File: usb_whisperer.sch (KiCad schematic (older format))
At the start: 2 parts, among them J1 Conn_01x04, J9 Conn_01x04

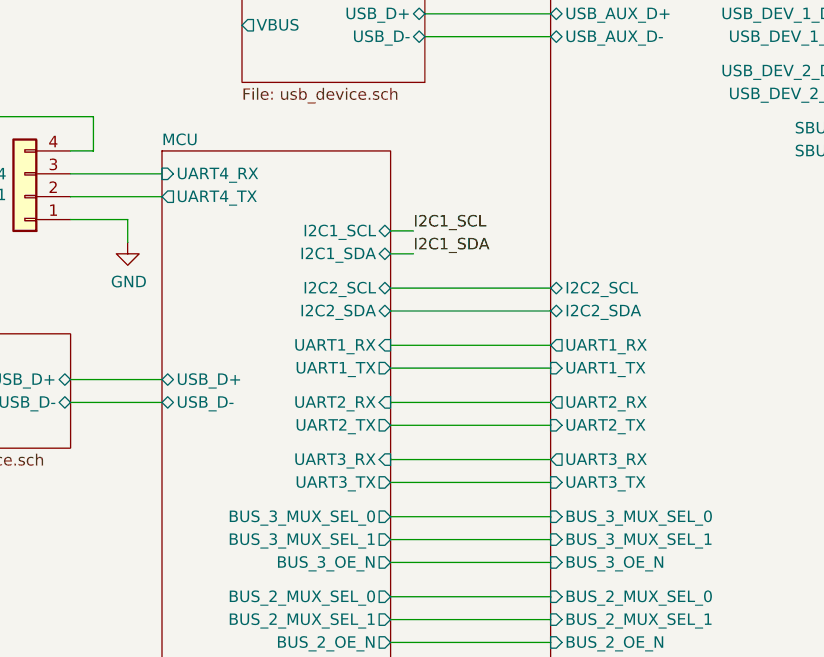
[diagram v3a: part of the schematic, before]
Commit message: Replace MCU by something available in distributors
Given the current chip shortage the STM32F0 was not available from
JLCPCB. This one (STM32F411CE) is available in large quantities from
JLCPCB. Despite being much more powerful than the F0, it is still in the
price range and actually cheaper than the STM32F103C8T6... which I don't
understand...
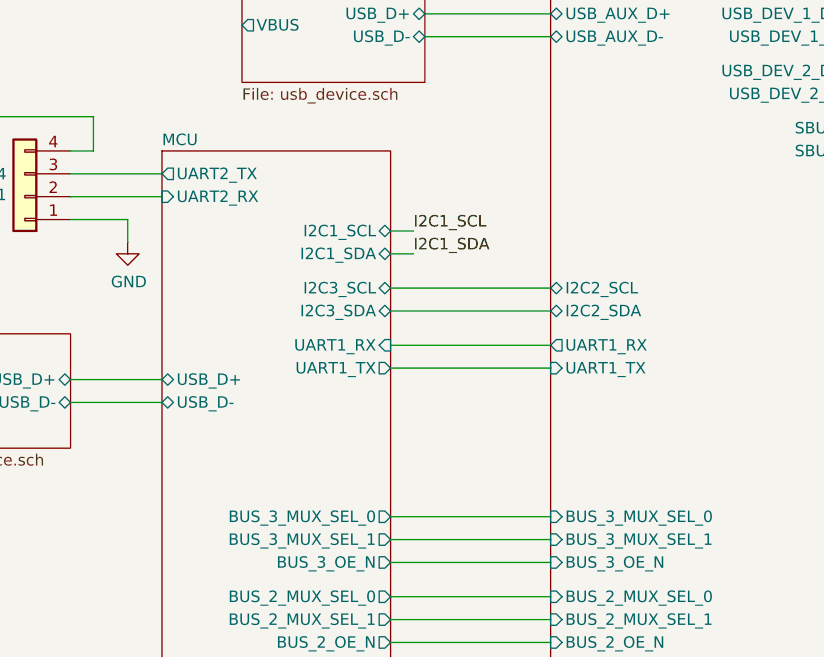
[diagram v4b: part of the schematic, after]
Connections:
- net MCU/UART4_RX is gone; now on net MCU/UART2_TX: J1.3 (Pin_3)
- net MCU/UART4_TX is gone; now on net MCU/UART2_RX: J1.2 (Pin_2)
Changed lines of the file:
@@
 F8 "UART1_TX" I L 5900 3850 50
 F9 "UART1_RX" O L 5900 3750 50
-F10 "UART2_TX" I L 5900 4100 50
-F11 "UART2_RX" O L 5900 4000 50
-F12 "UART3_TX" I L 5900 4350 50
-F13 "UART3_RX" O L 5900 4250 50
 F14 "I2C2_SCL" B L 5900 3500 50
 F15 "I2C2_SDA" B L 5900 3600 50
@@
 	5200 3850 5900 3850
 Wire Wire Line
-	5900 4000 5200 4000
-Wire Wire Line
-	5200 4100 5900 4100
-Wire Wire Line
 	7250 2300 8050 2300
 Wire Wire Line
@@
 Wire Wire Line
 	7650 3050 8050 3050
+Wire Wire Line
+	3800 3100 4200 3100
+Wire Wire Line
+	4200 3000 3800 3000
+$Comp
+L power:GND #PWR01
+U 1 1 61C1F3C5
+P 4050 3300
+F 0 "#PWR01" H 4050 3050 50  0001 C CNN
+F 1 "GND" H 4055 3127 50  0000 C CNN
+F 2 "" H 4050 3300 50  0001 C CNN
+F 3 "" H 4050 3300 50  0001 C CNN
+	1    4050 3300
+	1    0    0    -1
+$EndComp
+Wire Wire Line
+	4050 3300 4050 3200
+Wire Wire Line
+	4050 3200 3800 3200
+Wire Wire Line
+	5300 3250 5200 3250
+Wire Wire Line
+	5200 3350 5300 3350
+Wire Wire Line
+	5900 4500 5200 4500
+Wire Wire Line
+	5200 4600 5900 4600
+Wire Wire Line
+	5900 4700 5200 4700
+Wire Wire Line
+	5200 4850 5900 4850
+Wire Wire Line
+	5900 4950 5200 4950
+Wire Wire Line
+	5200 5050 5900 5050
+Wire Wire Line
+	5900 5200 5200 5200
+Wire Wire Line
+	5200 5300 5900 5300
+Wire Wire Line
+	5900 5400 5200 5400
+$Sheet
+S 2000 3750 550  400
+U 61EE6DE0
+F0 "Power" 50
+F1 "power.sch" 50
+F2 "VBUS" I R 2550 3950 50
+$EndSheet
+Wire Wire Line
+	3000 3950 2800 3950
+Wire Wire Line
+	3800 3900 4200 3900
+Wire Wire Line
+	4200 4000 3800 4000
+$Sheet
+S 4550 2100 800  500
+U 61AFE355
+F0 "USB_AUX" 50
+F1 "usb_device.sch" 50
+F2 "USB_D-" B R 5350 2400 50
+F3 "USB_D+" B R 5350 2300 50
+F4 "VBUS" O L 4550 2350 50
+$EndSheet
+Wire Wire Line
+	5900 2300 5350 2300
+Wire Wire Line
+	5350 2400 5900 2400
+Wire Wire Line
+	7900 6100 5200 6100
+Wire Wire Line
+	7900 3400 7900 6100
+Wire Wire Line
+	5200 5650 5900 5650
+Wire Wire Line
+	5200 5550 5900 5550
+Wire Wire Line
+	5200 5750 5900 5750
+Wire Wire Line
+	3900 2900 3800 2900
+Wire Wire Line
+	2800 2750 2800 3950
+Wire Wire Line
+	3900 2750 3900 2900
+Connection ~ 2800 3950
+Wire Wire Line
+	2800 3950 2550 3950
+$Comp
+L Connector_Generic:Conn_01x04 J9
+U 1 1 61A82B7E
+P 8550 4450
+F 0 "J9" H 8630 4442 50  0000 L CNN
+F 1 "Conn_01x04" H 8630 4351 50  0000 L CNN
+F 2 "" H 8550 4450 50  0001 C CNN
+F 3 "~" H 8550 4450 50  0001 C CNN
+	1    8550 4450
+	-1   0    0    1
+$EndComp
+Text Label 8850 4350 0    50   ~ 0
+I2C1_SDA
+Text Label 8850 4450 0    50   ~ 0
+I2C1_SCL
+Wire Wire Line
+	8750 4350 8850 4350
+Wire Wire Line
+	8850 4450 8750 4450
+$Comp
+L power:+3.3V #PWR010
+U 1 1 61A89DD5
+P 8850 4200
+F 0 "#PWR010" H 8850 4050 50  0001 C CNN
+F 1 "+3.3V" H 8865 4373 50  0000 C CNN
+F 2 "" H 8850 4200 50  0001 C CNN
+F 3 "" H 8850 4200 50  0001 C CNN
+	1    8850 4200
+	1    0    0    -1
+$EndComp
+$Comp
+L power:GND #PWR017
+U 1 1 61A8BB25
+P 8850 4600
+F 0 "#PWR017" H 8850 4350 50  0001 C CNN
+F 1 "GND" H 8855 4427 50  0000 C CNN
+F 2 "" H 8850 4600 50  0001 C CNN
+F 3 "" H 8850 4600 50  0001 C CNN
+	1    8850 4600
+	1    0    0    -1
+$EndComp
+Wire Wire Line
+	8850 4200 8850 4250
+Wire Wire Line
+	8850 4250 8750 4250
+Wire Wire Line
+	8750 4550 8850 4550
+Wire Wire Line
+	8850 4550 8850 4600
+$Sheet
+S 4200 2900 1000 3300
+U 61A89F2B
+F0 "MCU" 50
+F1 "mcu.sch" 50
+F2 "UART1_RX" I R 5200 3750 50
+F3 "USB_D+" B L 4200 3900 50
+F4 "USB_D-" B L 4200 4000 50
+F5 "I2C1_SCL" B R 5200 3250 50
+F6 "I2C1_SDA" B R 5200 3350 50
+F7 "USB_EV_N" I R 5200 6100 50
+F8 "BUS_1_OE_N" O R 5200 5400 50
+F9 "BUS_2_OE_N" O R 5200 5050 50
+F10 "BUS_3_OE_N" O R 5200 4700 50
+F11 "UART2_TX" O L 4200 3000 50
+F12 "UART2_RX" I L 4200 3100 50
+F13 "UART1_TX" O R 5200 3850 50
+F14 "BUS_1_MUX_SEL_0" O R 5200 5200 50
+F15 "BUS_2_MUX_SEL_0" O R 5200 4850 50
+F16 "BUS_3_MUX_SEL_0" O R 5200 4500 50
+F17 "BUS_1_MUX_SEL_1" O R 5200 5300 50
+F18 "BUS_2_MUX_SEL_1" O R 5200 4950 50
+F19 "BUS_3_MUX_SEL_1" O R 5200 4600 50
+F20 "USB_MUX_SEL_0" O R 5200 5550 50
+F21 "USB_MUX_SEL_1" O R 5200 5650 50
+F22 "USB_OE_N" O R 5200 5750 50
+F23 "I2C3_SCL" B R 5200 3500 50
+F24 "I2C3_SDA" B R 5200 3600 50
+$EndSheet
+Wire Wire Line
+	3900 2750 2800 2750
 $Comp
 L Connector_Generic:Conn_01x04 J1
@@
 	-1   0    0    1
 $EndComp
-Wire Wire Line
-	3800 3100 4200 3100
-Wire Wire Line
-	4200 3000 3800 3000
-$Comp
-L power:GND #PWR01
-U 1 1 61C1F3C5
-P 4050 3300
-F 0 "#PWR01" H 4050 3050 50  0001 C CNN
-F 1 "GND" H 4055 3127 50  0000 C CNN
-F 2 "" H 4050 3300 50  0001 C CNN
-F 3 "" H 4050 3300 50  0001 C CNN
-	1    4050 3300
-	1    0    0    -1
-$EndComp
-Wire Wire Line
-	4050 3300 4050 3200
-Wire Wire Line
-	4050 3200 3800 3200
-Wire Wire Line
-	5300 3250 5200 3250
-Wire Wire Line
-	5200 3350 5300 3350
-$Sheet
-S 4200 2900 1000 3300
-U 61A89F2B
-F0 "MCU" 50
-F1 "mcu.sch" 50
-F2 "UART1_RX" I R 5200 3750 50
-F3 "UART3_TX" O R 5200 4350 50
-F4 "UART3_RX" I R 5200 4250 50
-F5 "UART4_TX" O L 4200 3100 50
-F6 "UART4_RX" I L 4200 3000 50
-F7 "USB_D+" B L 4200 3900 50
-F8 "USB_D-" B L 4200 4000 50
-F9 "I2C1_SCL" B R 5200 3250 50
-F10 "I2C1_SDA" B R 5200 3350 50
-F11 "I2C2_SCL" B R 5200 3500 50
-F12 "I2C2_SDA" B R 5200 3600 50
-F13 "USB_EV_N" I R 5200 6100 50
-F14 "BUS_1_OE_N" O R 5200 5400 50
-F15 "BUS_2_OE_N" O R 5200 5050 50
-F16 "BUS_3_OE_N" O R 5200 4700 50
-F17 "UART2_TX" O R 5200 4100 50
-F18 "UART2_RX" I R 5200 4000 50
-F19 "UART1_TX" O R 5200 3850 50
-F20 "BUS_1_MUX_SEL_0" O R 5200 5200 50
-F21 "BUS_2_MUX_SEL_0" O R 5200 4850 50
-F22 "BUS_3_MUX_SEL_0" O R 5200 4500 50
-F23 "BUS_1_MUX_SEL_1" O R 5200 5300 50
-F24 "BUS_2_MUX_SEL_1" O R 5200 4950 50
-F25 "BUS_3_MUX_SEL_1" O R 5200 4600 50
-F26 "USB_MUX_SEL_0" O R 5200 5550 50
-F27 "USB_MUX_SEL_1" O R 5200 5650 50
-F28 "USB_OE_N" O R 5200 5750 50
-$EndSheet
-Wire Wire Line
-	5200 4250 5900 4250
-Wire Wire Line
-	5900 4350 5200 4350
-Wire Wire Line
-	5900 4500 5200 4500
-Wire Wire Line
-	5200 4600 5900 4600
-Wire Wire Line
-	5900 4700 5200 4700
-Wire Wire Line
-	5200 4850 5900 4850
-Wire Wire Line
-	5900 4950 5200 4950
-Wire Wire Line
-	5200 5050 5900 5050
-Wire Wire Line
-	5900 5200 5200 5200
-Wire Wire Line
-	5200 5300 5900 5300
-Wire Wire Line
-	5900 5400 5200 5400
-$Sheet
-S 2000 3750 550  400
-U 61EE6DE0
-F0 "Power" 50
-F1 "power.sch" 50
-F2 "VBUS" I R 2550 3950 50
-$EndSheet
-Wire Wire Line
-	3000 3950 2800 3950
-Wire Wire Line
-	3800 3900 4200 3900
-Wire Wire Line
-	4200 4000 3800 4000
-$Sheet
-S 4550 2100 800  500
-U 61AFE355
-F0 "USB_AUX" 50
-F1 "usb_device.sch" 50
-F2 "USB_D-" B R 5350 2400 50
-F3 "USB_D+" B R 5350 2300 50
-F4 "VBUS" O L 4550 2350 50
-$EndSheet
-Wire Wire Line
-	5900 2300 5350 2300
-Wire Wire Line
-	5350 2400 5900 2400
-Wire Wire Line
-	7900 6100 5200 6100
-Wire Wire Line
-	7900 3400 7900 6100
-Wire Wire Line
-	5200 5650 5900 5650
-Wire Wire Line
-	5200 5550 5900 5550
-Wire Wire Line
-	5200 5750 5900 5750
-Wire Wire Line
-	3900 2900 3800 2900
-Wire Wire Line
-	3900 2750 2800 2750
-Wire Wire Line
-	2800 2750 2800 3950
-Wire Wire Line
-	3900 2750 3900 2900
-Connection ~ 2800 3950
-Wire Wire Line
-	2800 3950 2550 3950
-$Comp
-L Connector_Generic:Conn_01x04 J9
-U 1 1 61A82B7E
-P 8550 4450
-F 0 "J9" H 8630 4442 50  0000 L CNN
-F 1 "Conn_01x04" H 8630 4351 50  0000 L CNN
-F 2 "" H 8550 4450 50  0001 C CNN
-F 3 "~" H 8550 4450 50  0001 C CNN
-	1    8550 4450
-	-1   0    0    1
-$EndComp
-Text Label 8850 4350 0    50   ~ 0
-I2C1_SDA
-Text Label 8850 4450 0    50   ~ 0
-I2C1_SCL
-Wire Wire Line
-	8750 4350 8850 4350
-Wire Wire Line
-	8850 4450 8750 4450
-$Comp
-L power:+3.3V #PWR010
-U 1 1 61A89DD5
-P 8850 4200
-F 0 "#PWR010" H 8850 4050 50  0001 C CNN
-F 1 "+3.3V" H 8865 4373 50  0000 C CNN
-F 2 "" H 8850 4200 50  0001 C CNN
-F 3 "" H 8850 4200 50  0001 C CNN
-	1    8850 4200
-	1    0    0    -1
-$EndComp
-$Comp
-L power:GND #PWR017
-U 1 1 61A8BB25
-P 8850 4600
-F 0 "#PWR017" H 8850 4350 50  0001 C CNN
-F 1 "GND" H 8855 4427 50  0000 C CNN
-F 2 "" H 8850 4600 50  0001 C CNN
-F 3 "" H 8850 4600 50  0001 C CNN
-	1    8850 4600
-	1    0    0    -1
-$EndComp
-Wire Wire Line
-	8850 4200 8850 4250
-Wire Wire Line
-	8850 4250 8750 4250
-Wire Wire Line
-	8750 4550 8850 4550
-Wire Wire Line
-	8850 4550 8850 4600
 $EndSCHEMATC
